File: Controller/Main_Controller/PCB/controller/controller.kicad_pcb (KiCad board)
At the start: 2 copper layers, 99.1 x 99.1 mm, 64 parts, among them J1 nRF24L01_Conn, Q1 S9013, Q2 S9013, Q3 S9013, SW1 SW_SPDT, U1 Joystick, U2 Joystick, U3 ZSR330GTA, U4 LM358DR2G, U5 ZLDO1117G50TA

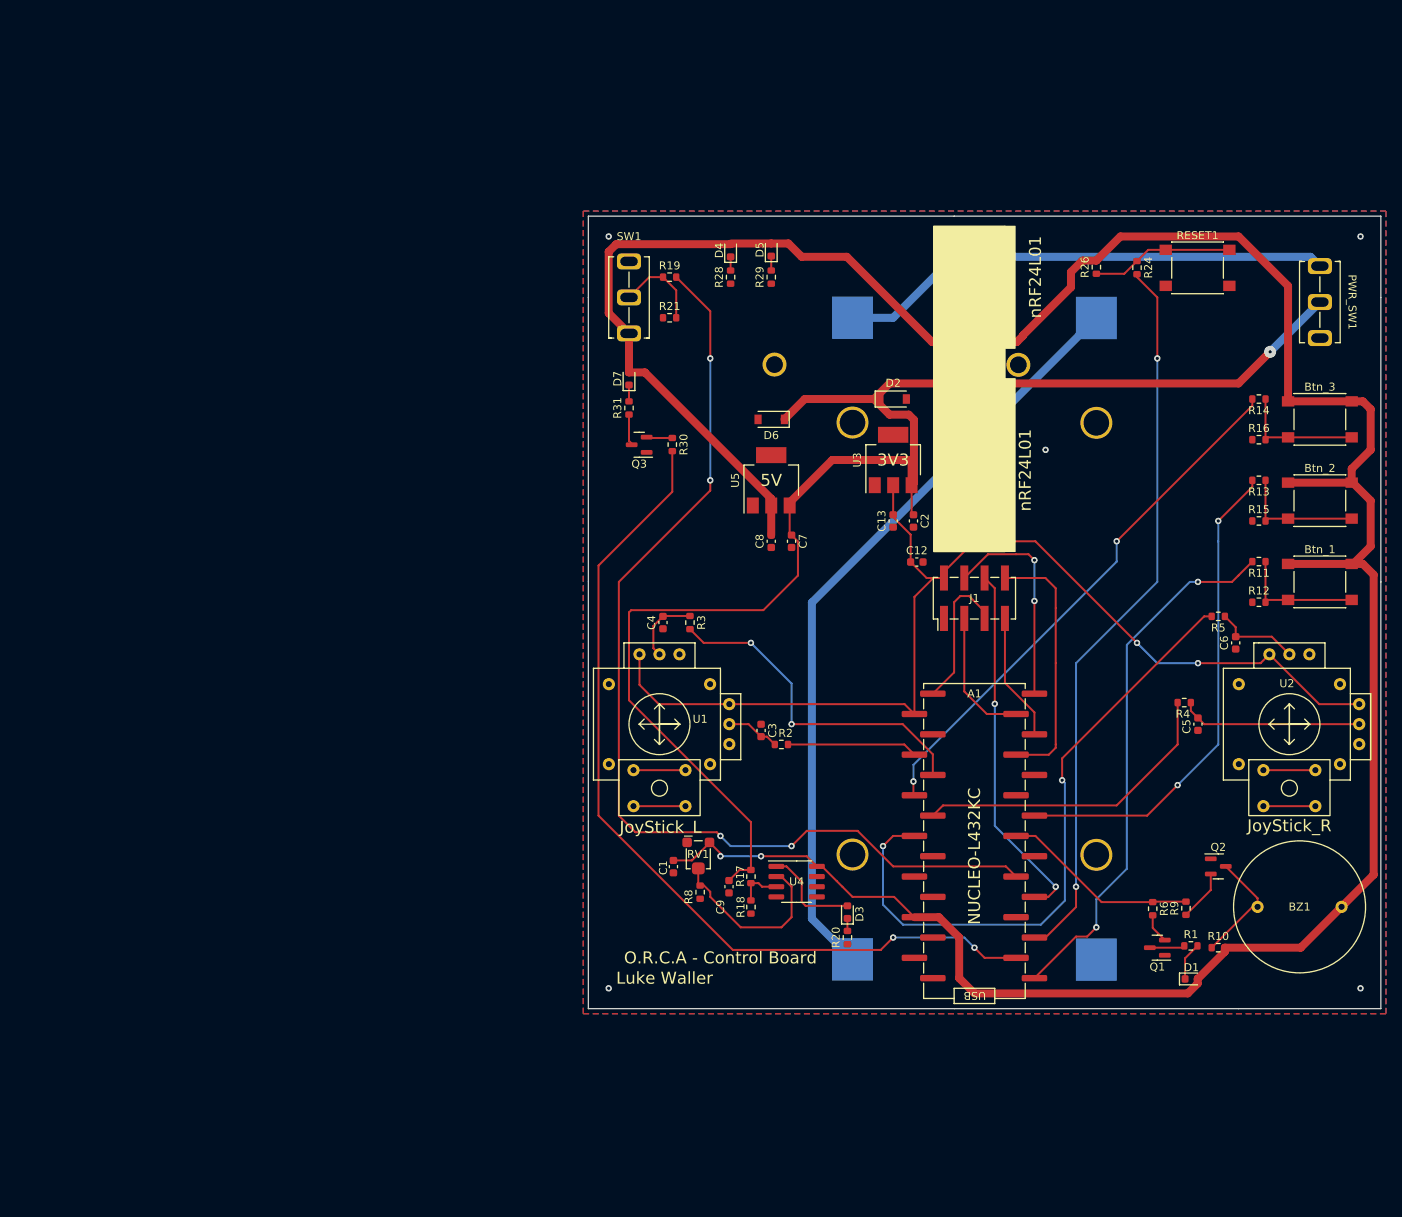
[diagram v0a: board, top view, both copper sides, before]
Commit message: Finished footprints on the schematic.
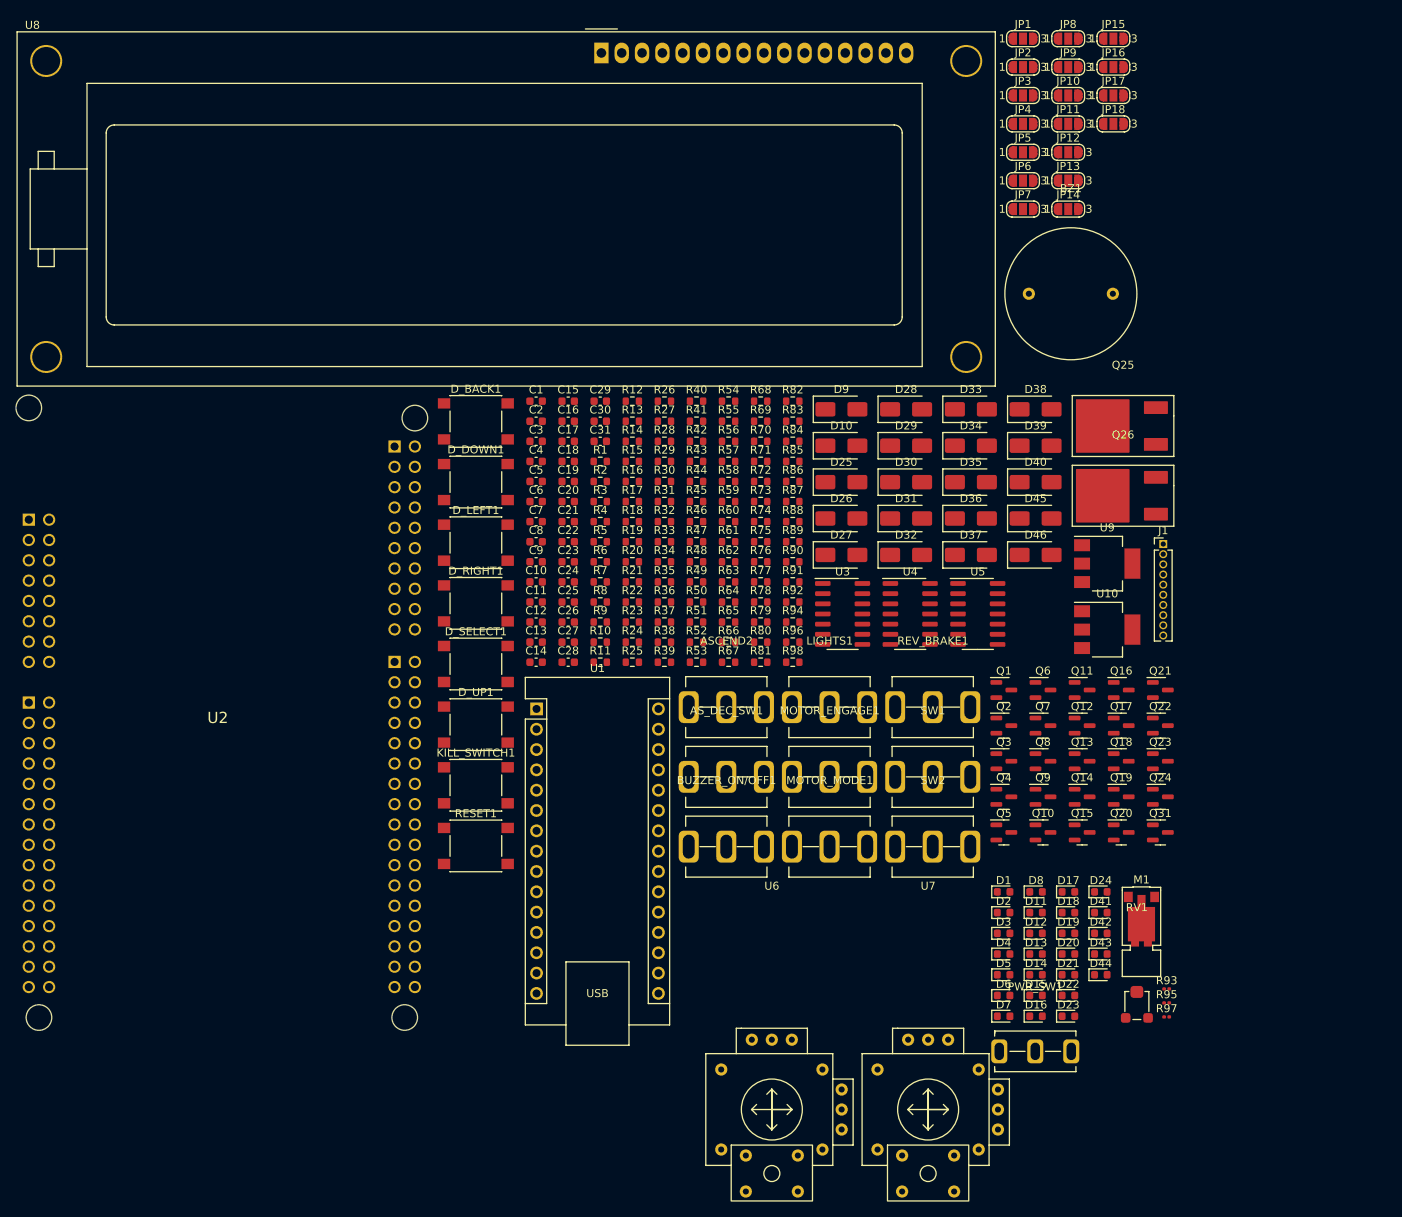
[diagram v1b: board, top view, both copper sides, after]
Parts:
- removed A1: NUCLEO-L432KC, My_library:NUCELO-L432KC_SMD
- removed BT1, BT2: Bat_18650, My_library:18650_Holder(1)
- removed Btn_1, Btn_2, Btn_3: SW_SPST, Button_Switch_SMD:SW_Push_1P1T_NO_6x6mm_H9.5mm
- added ASCEND2: SW_SPDT, My_library:1Ms1T1B1M1QE, F.Cu at (123.9, 112.2)
- added AS_DEC_SW1: SW_SPDT_MSM, My_library:1Ms1T1B1M1QE, F.Cu at (123.9, 120.9)
- added BUZZER_ON/OFF1: SW_SPDT, My_library:1Ms1T1B1M1QE, F.Cu at (123.9, 129.6)
- added C10: 100nF, Capacitor_SMD:C_0603_1608Metric, F.Cu at (100.2, 96.5)
- added C11: 100nF, Capacitor_SMD:C_0603_1608Metric, F.Cu at (100.2, 99.0)
- added C14: 100nF, Capacitor_SMD:C_0603_1608Metric, F.Cu at (100.2, 106.6)
- added C15: 100nF, Capacitor_SMD:C_0603_1608Metric, F.Cu at (104.2, 73.9)
- added C16: 100nF, Capacitor_SMD:C_0603_1608Metric, F.Cu at (104.2, 76.4)
- added C17: 100nF, Capacitor_SMD:C_0603_1608Metric, F.Cu at (104.2, 78.9)
- added C18: 100nF, Capacitor_SMD:C_0603_1608Metric, F.Cu at (104.2, 81.5)
- added C19: 100nF, Capacitor_SMD:C_0603_1608Metric, F.Cu at (104.2, 84.0)
- added C20: 100nF, Capacitor_SMD:C_0603_1608Metric, F.Cu at (104.2, 86.5)
- added C21: 100nF, Capacitor_SMD:C_0603_1608Metric, F.Cu at (104.2, 89.0)
- added C22: 100nF, Capacitor_SMD:C_0603_1608Metric, F.Cu at (104.2, 91.5)
- added C23: 100nF, Capacitor_SMD:C_0603_1608Metric, F.Cu at (104.2, 94.0)
- added C24: 100nF, Capacitor_SMD:C_0603_1608Metric, F.Cu at (104.2, 96.5)
- added C25: 100nF, Capacitor_SMD:C_0603_1608Metric, F.Cu at (104.2, 99.0)
- added C26: 100nF, Capacitor_SMD:C_0603_1608Metric, F.Cu at (104.2, 101.5)
- added C27: 100nF, Capacitor_SMD:C_0603_1608Metric, F.Cu at (104.2, 104.0)
- added C28: 100nF, Capacitor_SMD:C_0603_1608Metric, F.Cu at (104.2, 106.6)
- added C29: 100nF, Capacitor_SMD:C_0603_1608Metric, F.Cu at (108.2, 73.9)
- added C30: 100nF, Capacitor_SMD:C_0603_1608Metric, F.Cu at (108.2, 76.4)
- added C31: 100nF, Capacitor_SMD:C_0603_1608Metric, F.Cu at (108.2, 78.9)
- added D10: D, Diode_SMD:D_SMA, F.Cu at (138.3, 79.5)
- added D11: BLUE, LED_SMD:LED_0603_1608Metric, F.Cu at (162.6, 137.9)
- added D12: WHITE, LED_SMD:LED_0603_1608Metric, F.Cu at (162.6, 140.4)
- added D13: WHITE, LED_SMD:LED_0603_1608Metric, F.Cu at (162.6, 143.0)
- added D14: RED, LED_SMD:LED_0603_1608Metric, F.Cu at (162.6, 145.6)
- added D15: RED, LED_SMD:LED_0603_1608Metric, F.Cu at (162.6, 148.2)
- added D16: RED, LED_SMD:LED_0603_1608Metric, F.Cu at (162.6, 150.8)
- added D17: RED, LED_SMD:LED_0603_1608Metric, F.Cu at (166.7, 135.3)
- added D18: GREEN, LED_SMD:LED_0603_1608Metric, F.Cu at (166.7, 137.9)
- added D19: RED, LED_SMD:LED_0603_1608Metric, F.Cu at (166.7, 140.4)
- added D20: RED, LED_SMD:LED_0603_1608Metric, F.Cu at (166.7, 143.0)
- added D21: BLUE, LED_SMD:LED_0603_1608Metric, F.Cu at (166.7, 145.6)
- added D22: RED, LED_SMD:LED_0603_1608Metric, F.Cu at (166.7, 148.2)
- added D23: RED, LED_SMD:LED_0603_1608Metric, F.Cu at (166.7, 150.8)
- added D24: RED, LED_SMD:LED_0603_1608Metric, F.Cu at (170.7, 135.3)
- added D25: D, Diode_SMD:D_SMA, F.Cu at (138.3, 84.0)
- added D26: D, Diode_SMD:D_SMA, F.Cu at (138.3, 88.6)
- added D27: D, Diode_SMD:D_SMA, F.Cu at (138.3, 93.1)
- added D28: D, Diode_SMD:D_SMA, F.Cu at (146.4, 74.9)
- added D29: D, Diode_SMD:D_SMA, F.Cu at (146.4, 79.5)
- added D30: D, Diode_SMD:D_SMA, F.Cu at (146.4, 84.0)
- added D31: D, Diode_SMD:D_SMA, F.Cu at (146.4, 88.6)
- added D32: D, Diode_SMD:D_SMA, F.Cu at (146.4, 93.1)
- added D33: D, Diode_SMD:D_SMA, F.Cu at (154.5, 74.9)
- added D34: D, Diode_SMD:D_SMA, F.Cu at (154.5, 79.5)
- added D35: D, Diode_SMD:D_SMA, F.Cu at (154.5, 84.0)
- added D36: D, Diode_SMD:D_SMA, F.Cu at (154.5, 88.6)
- added D37: D, Diode_SMD:D_SMA, F.Cu at (154.5, 93.1)
- added D38: D, Diode_SMD:D_SMA, F.Cu at (162.6, 74.9)
- added D39: D, Diode_SMD:D_SMA, F.Cu at (162.6, 79.5)
- added D40: D, Diode_SMD:D_SMA, F.Cu at (162.6, 84.0)
- added D41: YELLOW, LED_SMD:LED_0603_1608Metric, F.Cu at (170.7, 137.9)
- added D42: BLUE, LED_SMD:LED_0603_1608Metric, F.Cu at (170.7, 140.4)
- added D43: GREEN, LED_SMD:LED_0603_1608Metric, F.Cu at (170.7, 143.0)
- added D44: BLUE, LED_SMD:LED_0603_1608Metric, F.Cu at (170.7, 145.6)
- added D45: D, Diode_SMD:D_SMA, F.Cu at (162.6, 88.6)
- added D46: D, Diode_SMD:D_SMA, F.Cu at (162.6, 93.1)
- added D8: RED, LED_SMD:LED_0603_1608Metric, F.Cu at (162.6, 135.3)
- added D9: D, Diode_SMD:D_SMA, F.Cu at (138.3, 74.9)
- added D_BACK1: SW_SPST, Button_Switch_SMD:SW_Push_1P1T_NO_6x6mm_H9.5mm, F.Cu at (92.6, 76.5)
- added D_DOWN1: SW_SPST, Button_Switch_SMD:SW_Push_1P1T_NO_6x6mm_H9.5mm, F.Cu at (92.6, 84.0)
- added D_LEFT1: SW_SPST, Button_Switch_SMD:SW_Push_1P1T_NO_6x6mm_H9.5mm, F.Cu at (92.6, 91.6)
- added D_RIGHT1: SW_SPST, Button_Switch_SMD:SW_Push_1P1T_NO_6x6mm_H9.5mm, F.Cu at (92.6, 99.2)
- added D_SELECT1: SW_SPST, Button_Switch_SMD:SW_Push_1P1T_NO_6x6mm_H9.5mm, F.Cu at (92.6, 106.8)
- added D_UP1: SW_SPST, Button_Switch_SMD:SW_Push_1P1T_NO_6x6mm_H9.5mm, F.Cu at (92.6, 114.4)
- added JP1: SolderJumper_3_Open, Jumper:SolderJumper-3_P1.3mm_Open_RoundedPad1.0x1.5mm_NumberLabels, F.Cu at (161.0, 28.6)
- added JP10: SolderJumper_3_Open, Jumper:SolderJumper-3_P1.3mm_Open_RoundedPad1.0x1.5mm_NumberLabels, F.Cu at (166.7, 35.7)
- added JP11: SolderJumper_3_Open, Jumper:SolderJumper-3_P1.3mm_Open_RoundedPad1.0x1.5mm_NumberLabels, F.Cu at (166.7, 39.3)
- added JP12: SolderJumper_3_Open, Jumper:SolderJumper-3_P1.3mm_Open_RoundedPad1.0x1.5mm_NumberLabels, F.Cu at (166.7, 42.8)
- added JP13: SolderJumper_3_Open, Jumper:SolderJumper-3_P1.3mm_Open_RoundedPad1.0x1.5mm_NumberLabels, F.Cu at (166.7, 46.4)
- added JP14: SolderJumper_3_Open, Jumper:SolderJumper-3_P1.3mm_Open_RoundedPad1.0x1.5mm_NumberLabels, F.Cu at (166.7, 49.9)
- added JP15: SolderJumper_3_Open, Jumper:SolderJumper-3_P1.3mm_Open_RoundedPad1.0x1.5mm_NumberLabels, F.Cu at (172.3, 28.6)
- added JP16: SolderJumper_3_Open, Jumper:SolderJumper-3_P1.3mm_Open_RoundedPad1.0x1.5mm_NumberLabels, F.Cu at (172.3, 32.2)
- added JP17: SolderJumper_3_Open, Jumper:SolderJumper-3_P1.3mm_Open_RoundedPad1.0x1.5mm_NumberLabels, F.Cu at (172.3, 35.7)
- added JP18: SolderJumper_3_Open, Jumper:SolderJumper-3_P1.3mm_Open_RoundedPad1.0x1.5mm_NumberLabels, F.Cu at (172.3, 39.3)
- added JP2: SolderJumper_3_Open, Jumper:SolderJumper-3_P1.3mm_Open_RoundedPad1.0x1.5mm_NumberLabels, F.Cu at (161.0, 32.2)
- added JP3: SolderJumper_3_Open, Jumper:SolderJumper-3_P1.3mm_Open_RoundedPad1.0x1.5mm_NumberLabels, F.Cu at (161.0, 35.7)
- added JP4: SolderJumper_3_Open, Jumper:SolderJumper-3_P1.3mm_Open_RoundedPad1.0x1.5mm_NumberLabels, F.Cu at (161.0, 39.3)
- added JP5: SolderJumper_3_Open, Jumper:SolderJumper-3_P1.3mm_Open_RoundedPad1.0x1.5mm_NumberLabels, F.Cu at (161.0, 42.8)
- added JP6: SolderJumper_3_Open, Jumper:SolderJumper-3_P1.3mm_Open_RoundedPad1.0x1.5mm_NumberLabels, F.Cu at (161.0, 46.4)
- added JP7: SolderJumper_3_Open, Jumper:SolderJumper-3_P1.3mm_Open_RoundedPad1.0x1.5mm_NumberLabels, F.Cu at (161.0, 49.9)
- added JP8: SolderJumper_3_Open, Jumper:SolderJumper-3_P1.3mm_Open_RoundedPad1.0x1.5mm_NumberLabels, F.Cu at (166.7, 28.6)
- added JP9: SolderJumper_3_Open, Jumper:SolderJumper-3_P1.3mm_Open_RoundedPad1.0x1.5mm_NumberLabels, F.Cu at (166.7, 32.2)
- added KILL_SWITCH1: SW_SPST, Button_Switch_SMD:SW_Push_1P1T_NO_6x6mm_H9.5mm, F.Cu at (92.6, 121.9)
- added LIGHTS1: SW_SPDT, My_library:1Ms1T1B1M1QE, F.Cu at (136.8, 112.2)
- added M1: Motor_DC, Motors:Vybronics_VZ30C1T8219732L, F.Cu at (175.8, 140.2)
- added MOTOR_ENGAGE1: SW_SPDT, My_library:1Ms1T1B1M1QE, F.Cu at (136.8, 120.9)
- added MOTOR_MODE1: SW_SPDT, My_library:1Ms1T1B1M1QE, F.Cu at (136.8, 129.6)
- added Q10: BC817, Package_TO_SOT_SMD:SOT-23, F.Cu at (163.5, 127.8)
- added Q11: BC817, Package_TO_SOT_SMD:SOT-23, F.Cu at (168.4, 110.0)
- added Q12: BC817, Package_TO_SOT_SMD:SOT-23, F.Cu at (168.4, 114.5)
- added Q13: BC817, Package_TO_SOT_SMD:SOT-23, F.Cu at (168.4, 118.9)
- added Q14: BC817, Package_TO_SOT_SMD:SOT-23, F.Cu at (168.4, 123.4)
- added Q15: BC817, Package_TO_SOT_SMD:SOT-23, F.Cu at (168.4, 127.8)
- added Q16: BC817, Package_TO_SOT_SMD:SOT-23, F.Cu at (173.3, 110.0)
- added Q17: BC817, Package_TO_SOT_SMD:SOT-23, F.Cu at (173.3, 114.5)
- added Q18: BC817, Package_TO_SOT_SMD:SOT-23, F.Cu at (173.3, 118.9)
- added Q19: BC817, Package_TO_SOT_SMD:SOT-23, F.Cu at (173.3, 123.4)
- added Q20: BC817, Package_TO_SOT_SMD:SOT-23, F.Cu at (173.3, 127.8)
- added Q21: BC817, Package_TO_SOT_SMD:SOT-23, F.Cu at (178.2, 110.0)
- added Q22: BC817, Package_TO_SOT_SMD:SOT-23, F.Cu at (178.2, 114.5)
- added Q23: BC817, Package_TO_SOT_SMD:SOT-23, F.Cu at (178.2, 118.9)
- added Q24: BC817, Package_TO_SOT_SMD:SOT-23, F.Cu at (178.2, 123.4)
- added Q25: IRFR9014PBF, My_library:STD20NF06L, F.Cu at (171.0, 77.0)
- added Q26: STD20NF06L, My_library:STD20NF06L, F.Cu at (171.0, 85.8)
- added Q31: BC817, Package_TO_SOT_SMD:SOT-23, F.Cu at (178.2, 127.8)
- added Q4: BC817, Package_TO_SOT_SMD:SOT-23, F.Cu at (158.6, 123.4)
- added Q5: BC817, Package_TO_SOT_SMD:SOT-23, F.Cu at (158.6, 127.8)
- added Q6: BC817, Package_TO_SOT_SMD:SOT-23, F.Cu at (163.5, 110.0)
- added Q7: BC817, Package_TO_SOT_SMD:SOT-23, F.Cu at (163.5, 114.5)
- added Q8: BC817, Package_TO_SOT_SMD:SOT-23, F.Cu at (163.5, 118.9)
- added Q9: BC817, Package_TO_SOT_SMD:SOT-23, F.Cu at (163.5, 123.4)
- added R22: 4K7, Resistor_SMD:R_0603_1608Metric, F.Cu at (112.2, 99.0)
- added R23: 4K7, Resistor_SMD:R_0603_1608Metric, F.Cu at (112.2, 101.5)
- added R25: 4K7, Resistor_SMD:R_0603_1608Metric, F.Cu at (112.2, 106.6)
- added R27: 1K, Resistor_SMD:R_0603_1608Metric, F.Cu at (116.2, 76.4)
- added R32: 150, Resistor_SMD:R_0603_1608Metric, F.Cu at (116.2, 89.0)
- added R33: 4K7, Resistor_SMD:R_0603_1608Metric, F.Cu at (116.2, 91.5)
- added R34: 4K7, Resistor_SMD:R_0603_1608Metric, F.Cu at (116.2, 94.0)
- added R35: 4K7, Resistor_SMD:R_0603_1608Metric, F.Cu at (116.2, 96.5)
- added R36: 4K7, Resistor_SMD:R_0603_1608Metric, F.Cu at (116.2, 99.0)
- added R37: 150, Resistor_SMD:R_0603_1608Metric, F.Cu at (116.2, 101.5)
- added R38: 2K2, Resistor_SMD:R_0603_1608Metric, F.Cu at (116.2, 104.0)
- added R39: 150, Resistor_SMD:R_0603_1608Metric, F.Cu at (116.2, 106.6)
- added R40: 150, Resistor_SMD:R_0603_1608Metric, F.Cu at (120.2, 73.9)
- added R41: 4K7, Resistor_SMD:R_0603_1608Metric, F.Cu at (120.2, 76.4)
- added R42: 4K7, Resistor_SMD:R_0603_1608Metric, F.Cu at (120.2, 78.9)
- added R43: 4K7, Resistor_SMD:R_0603_1608Metric, F.Cu at (120.2, 81.5)
- added R44: 4K7, Resistor_SMD:R_0603_1608Metric, F.Cu at (120.2, 84.0)
- added R45: 1K, Resistor_SMD:R_0603_1608Metric, F.Cu at (120.2, 86.5)
- added R46: 150, Resistor_SMD:R_0603_1608Metric, F.Cu at (120.2, 89.0)
- added R47: 150, Resistor_SMD:R_0603_1608Metric, F.Cu at (120.2, 91.5)
- added R48: 150, Resistor_SMD:R_0603_1608Metric, F.Cu at (120.2, 94.0)
- added R49: 47K, Resistor_SMD:R_0603_1608Metric, F.Cu at (120.2, 96.5)
- added R50: 47K, Resistor_SMD:R_0603_1608Metric, F.Cu at (120.2, 99.0)
- added R51: 47K, Resistor_SMD:R_0603_1608Metric, F.Cu at (120.2, 101.5)
- added R52: 47K, Resistor_SMD:R_0603_1608Metric, F.Cu at (120.2, 104.0)
- added R53: 47K, Resistor_SMD:R_0603_1608Metric, F.Cu at (120.2, 106.6)
- added R54: 47K, Resistor_SMD:R_0603_1608Metric, F.Cu at (124.2, 73.9)
- added R55: 47K, Resistor_SMD:R_0603_1608Metric, F.Cu at (124.2, 76.4)
- added R56: 47K, Resistor_SMD:R_0603_1608Metric, F.Cu at (124.2, 78.9)
- added R57: 47K, Resistor_SMD:R_0603_1608Metric, F.Cu at (124.2, 81.5)
- added R58: 47K, Resistor_SMD:R_0603_1608Metric, F.Cu at (124.2, 84.0)
- added R59: 47K, Resistor_SMD:R_0603_1608Metric, F.Cu at (124.2, 86.5)
- added R60: 47K, Resistor_SMD:R_0603_1608Metric, F.Cu at (124.2, 89.0)
- added R61: 47K, Resistor_SMD:R_0603_1608Metric, F.Cu at (124.2, 91.5)
- added R62: 47K, Resistor_SMD:R_0603_1608Metric, F.Cu at (124.2, 94.0)
- added R63: 47K, Resistor_SMD:R_0603_1608Metric, F.Cu at (124.2, 96.5)
- added R64: 47K, Resistor_SMD:R_0603_1608Metric, F.Cu at (124.2, 99.0)
- added R65: 47K, Resistor_SMD:R_0603_1608Metric, F.Cu at (124.2, 101.5)
- added R66: 47K, Resistor_SMD:R_0603_1608Metric, F.Cu at (124.2, 104.0)
- added R67: 47K, Resistor_SMD:R_0603_1608Metric, F.Cu at (124.2, 106.6)
- added R68: 47K, Resistor_SMD:R_0603_1608Metric, F.Cu at (128.2, 73.9)
- added R69: 47K, Resistor_SMD:R_0603_1608Metric, F.Cu at (128.2, 76.4)
- added R7: 4K7, Resistor_SMD:R_0603_1608Metric, F.Cu at (108.2, 96.5)
- added R70: 47K, Resistor_SMD:R_0603_1608Metric, F.Cu at (128.2, 78.9)
- added R71: 47K, Resistor_SMD:R_0603_1608Metric, F.Cu at (128.2, 81.5)
- added R72: 47K, Resistor_SMD:R_0603_1608Metric, F.Cu at (128.2, 84.0)
- added R73: 47K, Resistor_SMD:R_0603_1608Metric, F.Cu at (128.2, 86.5)
- added R74: 47K, Resistor_SMD:R_0603_1608Metric, F.Cu at (128.2, 89.0)
- added R75: 620, Resistor_SMD:R_0603_1608Metric, F.Cu at (128.2, 91.5)
- added R76: 620, Resistor_SMD:R_0603_1608Metric, F.Cu at (128.2, 94.0)
- added R77: 620, Resistor_SMD:R_0603_1608Metric, F.Cu at (128.2, 96.5)
- added R78: 620, Resistor_SMD:R_0603_1608Metric, F.Cu at (128.2, 99.0)
- added R79: 47K, Resistor_SMD:R_0603_1608Metric, F.Cu at (128.2, 101.5)
- added R80: 47K, Resistor_SMD:R_0603_1608Metric, F.Cu at (128.2, 104.0)
- added R81: 47K, Resistor_SMD:R_0603_1608Metric, F.Cu at (128.2, 106.6)
- added R82: 47K, Resistor_SMD:R_0603_1608Metric, F.Cu at (132.2, 73.9)
- added R83: 47K, Resistor_SMD:R_0603_1608Metric, F.Cu at (132.2, 76.4)
- added R84: 47K, Resistor_SMD:R_0603_1608Metric, F.Cu at (132.2, 78.9)
- added R85: 2K2, Resistor_SMD:R_0603_1608Metric, F.Cu at (132.2, 81.5)
- added R86: 1K, Resistor_SMD:R_0603_1608Metric, F.Cu at (132.2, 84.0)
- added R87: 4K7, Resistor_SMD:R_0603_1608Metric, F.Cu at (132.2, 86.5)
- added R88: 2K2, Resistor_SMD:R_0603_1608Metric, F.Cu at (132.2, 89.0)
- added R89: 2K2, Resistor_SMD:R_0603_1608Metric, F.Cu at (132.2, 91.5)
- added R90: 1K, Resistor_SMD:R_0603_1608Metric, F.Cu at (132.2, 94.0)
- added R91: 10K, Resistor_SMD:R_0603_1608Metric, F.Cu at (132.2, 96.5)
- added R92: 4K7, Resistor_SMD:R_0603_1608Metric, F.Cu at (132.2, 99.0)
- added R93: 1K, Resistor_SMD:R_0201_0603Metric, F.Cu at (179.0, 147.4)
- added R94: 4K7, Resistor_SMD:R_0603_1608Metric, F.Cu at (132.2, 101.5)
- added R95: 100K, Resistor_SMD:R_0201_0603Metric, F.Cu at (179.0, 149.1)
- added R96: 220R, Resistor_SMD:R_0603_1608Metric, F.Cu at (132.2, 104.0)
- added R97: 100R, Resistor_SMD:R_0201_0603Metric, F.Cu at (179.0, 150.9)
- added R98: 10K, Resistor_SMD:R_0603_1608Metric, F.Cu at (132.2, 106.6)
- added REV_BRAKE1: SW_SPDT, My_library:1Ms1T1B1M1QE, F.Cu at (149.7, 112.2)
- added SW2: SW_SPDT, My_library:1Ms1T1B1M1QE, F.Cu at (149.7, 129.6)
- added U10: ZLDO1117G50TA, Package_TO_SOT_SMD:SOT-223, F.Cu at (171.5, 102.5)
- added U6: Joystick, My_library:Joystick, F.Cu at (129.6, 162.5)
- added U7: Joystick, My_library:Joystick, F.Cu at (149.2, 162.5)
- added U8: HY1602E, Display:HY1602E, F.Cu at (108.3, 30.4)
- added U9: ZSR330GTA, Package_TO_SOT_SMD:SOT-223, F.Cu at (171.5, 94.2)
- D1: value GREEN -> BLUE
- D2, D6: value B5817W-5819W -> GREEN; footprint Diode_SMD:D_SOD-123 -> LED_SMD:LED_0603_1608Metric
- D3, D4: value YELLOW -> RED
- D5: value BLUE -> WHITE
- D7: value BLUE -> RED
- J1: value nRF24L01_Conn -> Conn_01x10; footprint Connector_PinHeader_2.54mm:PinHeader_2x04_P2.54mm_Vertical_SMD -> Connector_PinHeader_1.27mm:PinHeader_1x10_P1.27mm_Vertical
- Q1, Q2, Q3: value S9013 -> BC817
- R1, R24: value 2K2 -> 4K7
- R10, R21, R26: value 10K -> 4K7
- R11: value 2K2 -> 150
- R12, R15, R16: value 10K -> 150
- R13, R28: value 2K2 -> 390
- R17, R18: value 100K -> 47K
- R19, R20: value 2K2 -> 47K
- R2: value 620 -> 1K
- R29: value 1K -> 390
- R3, R5: value 620 -> 4K7
- R30: value 4K7 -> 150
- R31: value 1K -> 150
- R4: value 620 -> 2K2
- R8: value 40K -> 4K7
- SW1: footprint My_library:KNX-1-D1 -> My_library:1Ms1T1B1M1QE
- U1: value Joystick -> NUCLEO-L432KC; footprint My_library:Joystick -> Module:Arduino_Nano
- U2: value Joystick -> NUCLEO144-F429ZI; footprint My_library:Joystick -> My_library:MODULE_NUCLEO-F429ZI_JUST_PINS
- U3: value ZSR330GTA -> 74HC14; footprint Package_TO_SOT_SMD:SOT-223 -> Package_SO:SO-14_3.9x8.65mm_P1.27mm
- U4: value LM358DR2G -> 74HC14; footprint Package_SO:SOP-8_3.76x4.96mm_P1.27mm -> Package_SO:SO-14_3.9x8.65mm_P1.27mm
- U5: value ZLDO1117G50TA -> 74HC14; footprint Package_TO_SOT_SMD:SOT-223 -> Package_SO:SO-14_3.9x8.65mm_P1.27mm
- moved U2 133.4 mm to (60.9, 113.5)
- moved RESET1 115.6 mm to (92.6, 129.5)
- moved PWR_SW1 100.2 mm to (162.5, 155.2), turned to 0 degrees
- moved R1 95.5 mm to (108.2, 81.5)
- moved D5 95.2 mm to (158.6, 145.6), turned to 0 degrees
- moved D4 94.3 mm to (158.6, 143.0), turned to 0 degrees
- moved D7 92.4 mm to (158.6, 150.8), turned to 0 degrees
- moved C6 89.2 mm to (100.2, 86.5), turned to 0 degrees
- moved C5 88.1 mm to (100.2, 84.0), turned to 0 degrees
- moved R10 86.2 mm to (108.2, 104.0)
- moved R11 83.3 mm to (108.2, 106.6), turned to 0 degrees
- moved R12 82.3 mm to (112.2, 73.9)
- moved BZ1 81.8 mm to (167.0, 60.5), turned to 0 degrees
- moved R6 81.5 mm to (108.2, 94.0), turned to 0 degrees
- moved R9 81.5 mm to (108.2, 101.5), turned to 0 degrees
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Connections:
- BZ1 pad 1: +5V -> Net-(BUZZER_ON/OFF1-A)
- BZ1 pad 2: Net-(BZ1-Pad2) -> Net-(BZ1-+)
- C1 pad 1: +5V -> Earth
- C1 pad 2: Earth -> SWITCH_1_SB
- C12 pad 1: +3V3 -> Earth
- C12 pad 2: Earth -> MOTOR_DENGAGE_SB
- C13 pad 1: Earth -> +3V3
- C13 pad 2: +3V3 -> Earth
- C2 pad 1: BAT_PWR -> Earth
- C2 pad 2: Earth -> SWITCH_2_SB
- C3 pad 2: Net-(C3-Pad2) -> MOTOR_MODE_1_SB
- C4 pad 2: Net-(C4-Pad2) -> MOTOR_MODE_2_SB
- C5 pad 2: Net-(C5-Pad2) -> KILL_SWITCH_SB
- C6 pad 2: Net-(C6-Pad2) -> ASCEND_SB
- C7 pad 1: BAT_PWR -> Earth
- C7 pad 2: Earth -> DESCEND_SB
- C8 pad 2: +5V -> LIGHTS_SB
- C9 pad 1: BAT_PWR -> Earth
- C9 pad 2: Earth -> BRAKE_MODE_SB
- D1 pad 1: Net-(D1-Pad1) -> Net-(D1-K)
- D2 pad 1: BAT_PWR -> Net-(D2-K)
- D2 pad 2: Earth -> +5V
- D3 pad 1: Net-(D3-Pad1) -> Net-(D3-K)
- D3 pad 2: Net-(D3-Pad2) -> +5V
- D4 pad 1: Net-(D4-Pad1) -> Net-(D4-K)
- D5 pad 1: Net-(D5-Pad1) -> Net-(D5-K)
- D6 pad 1: BAT_PWR -> Net-(D6-K)
- D6 pad 2: Earth -> +5V
- D7 pad 1: Net-(D7-Pad1) -> Net-(D7-K)
- J1 pad 1: Earth -> VIN
- J1 pad 2: +3V3 -> MOSI_1
- J1 pad 3: NRF_CE -> MISO_1
- J1 pad 4: NRF_CSN -> CLK_1
- J1 pad 5: NRF_SCK -> MOSI_2
- J1 pad 6: NRF_MOSI -> MISO_2
- J1 pad 7: NRF_MISO -> CLK_2
- J1 pad 8: NRF_IRQ -> DET_IN
- PWR_SW1 pad 1: +BATT -> +12V
- PWR_SW1 pad 2: BAT_PWR -> Net-(D45-K)
- Q1 pad 1: Earth -> Net-(Q1-B)
- Q1 pad 2: Net-(Q1-Pad2) -> Earth
- Q1 pad 3: Net-(Q1-Pad3) -> Net-(Q1-C)
- Q2 pad 1: Earth -> Net-(Q2-B)
- Q2 pad 2: Net-(Q2-Pad2) -> Earth
- Q2 pad 3: Net-(BZ1-Pad2) -> Net-(Q2-C)
- Q3 pad 1: Earth -> Net-(Q3-B)
- Q3 pad 2: Net-(Q3-Pad2) -> Earth
- Q3 pad 3: Net-(Q3-Pad3) -> Net-(Q3-C)
- R1 pad 1: Net-(Q1-Pad3) -> Net-(Q1-B)
- R1 pad 2: Net-(D1-Pad1) -> MOTOR_MODE_1_LED
- R10 pad 1: Net-(BZ1-Pad2) -> Net-(Q18-B)
- R10 pad 2: +5V -> COL_SENS_7
- R11 pad 1: Net-(Btn_1-Pad2) -> Net-(Q3-C)
- R11 pad 2: Btn_1 -> Net-(D3-K)
- R12 pad 1: Earth -> Net-(Q4-C)
- R12 pad 2: Net-(Btn_1-Pad2) -> Net-(D4-K)
- R13 pad 1: Net-(Btn_2-Pad2) -> Net-(Q5-C)
- R13 pad 2: Btn_2 -> Net-(D5-K)
- R14 pad 1: Net-(Btn_3-Pad2) -> Net-(Q6-C)
- R14 pad 2: Btn_3 -> Net-(D6-K)
- R15 pad 1: Earth -> Net-(Q7-C)
- R15 pad 2: Net-(Btn_2-Pad2) -> Net-(D7-K)
- R16 pad 1: Earth -> Net-(Q18-C)
- R16 pad 2: Net-(Btn_3-Pad2) -> Net-(D8-K)
- R17 pad 1: Net-(R17-Pad1) -> Net-(D9-A)
- R17 pad 2: BAT_PWR -> +5V
- R18 pad 1: Earth -> Net-(D10-A)
- R18 pad 2: Net-(R17-Pad1) -> +5V
- R19 pad 1: Net-(R19-Pad1) -> SWITCH_1_SB
- R19 pad 2: SW_1 -> Net-(D9-A)
- R2 pad 1: Net-(C3-Pad2) -> Net-(Q1-C)
- R2 pad 2: L_PITCH -> Net-(D1-K)
- R20 pad 1: Earth -> SWITCH_2_SB
- R20 pad 2: Net-(D3-Pad1) -> Net-(D10-A)
- R21 pad 1: Earth -> Net-(Q9-B)
- R21 pad 2: Net-(R19-Pad1) -> ASCEND_LED
- R24 pad 1: Net-(R24-Pad1) -> Net-(Q12-B)
- R24 pad 2: RESET -> LED_2
- R26 pad 1: Net-(R24-Pad1) -> Net-(Q22-B)
- R26 pad 2: +5V -> COL_SENS_8
- R28 pad 1: Earth -> Net-(Q10-C)
- R28 pad 2: Net-(D4-Pad1) -> Net-(D12-K)
- R29 pad 1: Earth -> Net-(Q11-C)
- R29 pad 2: Net-(D5-Pad1) -> Net-(D13-K)
- R3 pad 1: Net-(C4-Pad2) -> Net-(Q2-B)
- R3 pad 2: L_ROLL -> MOTOR_MODE_2_LED
- R30 pad 1: Net-(Q3-Pad2) -> Net-(Q12-C)
- R30 pad 2: LED_1 -> Net-(D14-K)
- R31 pad 1: Net-(Q3-Pad3) -> Net-(Q8-C)
- R31 pad 2: Net-(D7-Pad1) -> Net-(D15-K)
- R4 pad 1: Net-(C5-Pad2) -> Net-(Q2-C)
- R4 pad 2: R_PITCH -> Net-(D2-K)
- R5 pad 1: Net-(C6-Pad2) -> Net-(Q3-B)
- R5 pad 2: R_ROLL -> KILL_SWTICH_LED
- R6 pad 1: BUZZER -> Net-(Q4-B)
- R6 pad 2: Net-(Q1-Pad2) -> BRAKE_LED
- R8 pad 1: Earth -> Net-(Q6-B)
- R8 pad 2: Net-(R8-Pad2) -> LED_1
- R9 pad 1: Net-(Q2-Pad2) -> Net-(Q7-B)
- R9 pad 2: BUZZER -> COL_SENS_3
- RESET1 pad 1: Net-(R24-Pad1) -> Net-(RESET1-A)
- RV1 pad 1: +5V -> Earth
- RV1 pad 2: Net-(R8-Pad2) -> Net-(U8-Vo)
- RV1 pad 3: Earth -> +5V
- SW1 pad 1: +5V -> Net-(D9-A)
- SW1 pad 2: Net-(R19-Pad1) -> Earth
- U3 pad 1: Earth -> MOTOR_MODE_1_SB
- U3 pad 2: +3V3 -> MOTOR_MODE_1
- U3 pad 3: BAT_PWR -> MOTOR_MODE_2_SB
- U3 pad 4: (no net) -> MOTOR_MODE_2
- U4 pad 1: Net-(D3-Pad2) -> BRAKE_MODE_SB
- U4 pad 2: Net-(R8-Pad2) -> BRAKE_MODE
- U4 pad 3: Net-(R17-Pad1) -> REV_MODE_SB
- U4 pad 4: Earth -> REV_MODE
- U4 pad 5: unconnected-(U4-Pad5) -> MOTOR_ENGAGE_SB
- U4 pad 6: unconnected-(U4-Pad6) -> MOTOR_EN
- U4 pad 7: unconnected-(U4-Pad7) -> Earth
- U4 pad 8: +5V -> MOTOR_DE
- U5 pad 1: Earth -> D_UP_SB
- U5 pad 2: +5V -> D_UP
- U5 pad 3: BAT_PWR -> D_DOWN_SB
- U5 pad 4: (no net) -> D_DOWN
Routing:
- net +5V: track 355.1 -> 0.00 mm, vias 2 -> 0
- net BAT_PWR: track 186.1 -> 0.00 mm, vias 1 -> 0
- net +3V3: track 138.1 -> 0.00 mm, vias 2 -> 0
- net SW_1: track 128.2 -> 0.00 mm, vias 4 -> 0
- net LED_1: track 110.2 -> 0.00 mm, vias 2 -> 0
- net Net-(BT1-Pad2): track 97.0 -> 0.00 mm
- net RESET: track 91.1 -> 0.00 mm, vias 2 -> 0
- net R_ROLL: track 80.8 -> 0.00 mm, vias 2 -> 0
- net Btn_1: track 67.3 -> 0.00 mm, vias 2 -> 0
- net Btn_3: track 67.1 -> 0.00 mm, vias 2 -> 0
- net +BATT: track 62.1 -> 0.00 mm
- net Btn_2: track 61.4 -> 0.00 mm, vias 2 -> 0
- net NRF_MOSI: track 45.7 -> 0.00 mm, vias 2 -> 0
- net L_ROLL: track 42.4 -> 0.00 mm, vias 2 -> 0
- net R_PITCH: track 39.5 -> 0.00 mm
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- removed copper zone on B.Cu, net Earth
- removed copper zone on F.Cu, net Earth
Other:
- board outline removed
- board text removed: "3V3"
- board text removed: "5V"
- board text removed: "JoyStick_L"
- board text removed: "JoyStick_R"
- board text removed: "Luke Waller"
- board text removed: "NUCLEO-L432KC"
- board text removed: "O.R.C.A - Control Board"
- board text removed: "nRF24L01"

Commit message: PCB design
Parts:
- KILL_SWITCH1: footprint Button_Switch_SMD:SW_Push_1P1T_NO_6x6mm_H9.5mm -> My_library:Toggle_Switch_10TC605
- Q13, Q14, Q17, Q18, Q21, Q22, Q7, Q8, R10, R25, R26, R35, R36, R43, R44, R9, U1, U2, U5: moved to B.Cu
- R11, R12, R30, R37, R46: value 150 -> 150R
- R13, R28, R29: value 390 -> 390R
- R15, R16, R31, R32, R39, R40, R47, R48: value 150 -> 150R; moved to B.Cu
- R75, R76, R77, R78: value 620 -> 620R
- U8: footprint Display:HY1602E -> My_library:LCD_Display_WH1602B-NYG-JT
- moved R45 302.3 mm to (393.7, -42.4), turned to 90 degrees
- moved R37 298.7 mm to (398.0, 2.54)
- moved R52 297.8 mm to (394.2, -12.7)
- moved D21 297.2 mm to (393.7, -46.2), turned to 90 degrees
- moved R41 295.8 mm to (389.1, -47.0), turned to 180 degrees
- moved C8 295.5 mm to (363.2, -43.2)
- moved C7 294.9 mm to (376.0, -15.2)
- moved R33 291.9 mm to (394.2, 2.54)
- moved C6 290.7 mm to (374.7, -8.89)
- moved AS_DEC_SW1 289.5 mm to (384.0, -6.35)
- moved LIGHTS1 286.9 mm to (378.8, -41.9)
- moved R62 286.3 mm to (393.8, -2.54)
- moved R53 284.1 mm to (384.1, 1.27)
- moved R63 282.7 mm to (390.0, 0.00)
- moved R64 282.4 mm to (368.2, -43.2)
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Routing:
- net D_BACK_SB: track 0.00 -> 93.3 mm, vias 0 -> 1
- net Net-(D39-A): track 0.00 -> 81.9 mm
- net D_DOWN_SB: track 0.00 -> 78.2 mm, vias 0 -> 1
- net D_LEFT_SB: track 0.00 -> 78.2 mm, vias 0 -> 1
- net D_RIGHT_SB: track 0.00 -> 55.3 mm, vias 0 -> 1
- net Net-(BZ1-+): track 0.00 -> 45.6 mm
- net D_UP_SB: track 0.00 -> 41.8 mm, vias 0 -> 1
- net Net-(Q24-C): track 0.00 -> 28.0 mm
- net LCD_D7: track 0.00 -> 27.1 mm
- net Net-(D36-A): track 0.00 -> 27.1 mm
- net Net-(BUZZER_ON/OFF1-A): track 0.00 -> 25.3 mm
- net LCD_D6: track 0.00 -> 25.0 mm
- net LCD_D4: track 0.00 -> 25.0 mm
- net LCD_D5: track 0.00 -> 25.0 mm
- net LCD_RS: track 0.00 -> 25.0 mm
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
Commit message: Tracings complete for the PCB.
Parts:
- added JP19: Jumper_2_Open, My_library:Jumper, F.Cu at (157.0, 24.3)
- added JP20: SolderJumper_2_Open, Jumper:SolderJumper-2_P1.3mm_Open_RoundedPad1.0x1.5mm, F.Cu at (153.6, 24.3)
- KILL_SWITCH1: value SW_SPST -> SW_SPDT; footprint My_library:Toggle_Switch_10TC605 -> My_library:1Ms1T1B1M1QE
- R93, R95, R97: footprint Resistor_SMD:R_0201_0603Metric -> Resistor_SMD:R_0603_1608Metric
- moved D28 293.3 mm to (103.2, 21.8)
- moved R62 292.3 mm to (103.1, 28.1)
- moved R63 290.7 mm to (103.1, 47.2)
- moved R37 287.3 mm to (114.1, 46.4), turned to 90 degrees
- moved R52 287.0 mm to (109.4, 23.1), turned to 90 degrees
- moved D17 286.9 mm to (109.5, 44.7), turned to 180 degrees
- moved Q15 285.8 mm to (115.3, 50.7), turned to 180 degrees
- moved C7 283.9 mm to (98.1, 42.9), turned to -90 degrees
- moved AS_DEC_SW1 283.4 mm to (103.9, 37.0), turned to -90 degrees
- moved C6 279.9 mm to (97.6, 30.2), turned to 90 degrees
- moved R53 279.1 mm to (109.4, 51.0), turned to -90 degrees
- moved R33 278.4 mm to (119.2, 45.5), turned to 90 degrees
- moved JP11 278.2 mm to (96.3, 49.8), turned to -90 degrees
- moved D29 278.0 mm to (103.2, 53.5)
- moved JP7 273.6 mm to (96.3, 23.1), turned to 90 degrees
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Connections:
- J1 pad 8: DET_IN -> Net-(J1-Pin_8)
- J1 pad 9: DET_OUT -> Net-(J1-Pin_9)
- KILL_SWITCH1 pad 1: Earth -> Net-(D27-A)
- KILL_SWITCH1 pad 2: Net-(D27-A) -> Earth
- KILL_SWITCH1 pad 3: (no net) -> unconnected-(KILL_SWITCH1-C-Pad3)
- R5 pad 2: KILL_SWTICH_LED -> KILL_LED
- U1 pad 15: D_SELECT -> D_SEL
- U2 pad 1: BRAKE_LED -> REV_LED
- U2 pad 108: KILL_LED -> MOTOR_DE
- U2 pad 109: L_PITCH -> R_ROLL
- U2 pad 114: KILL_SWITCH -> MOTOR_EN
- U2 pad 115: unconnected-(U2-PD12-Pad115) -> COL_SENS_2
- U2 pad 116: COL_SENS_8 -> COL_SENS_1
- U2 pad 117: COL_SENS_2 -> COL_SENS_4
- U2 pad 119: COL_SENS_6 -> COL_SENS_3
- U2 pad 123: COL_SENS_4 -> COL_SENS_5
- U2 pad 125: COL_SENS_3 -> COL_SENS_6
- U2 pad 128: COL_SENS_5 -> COL_SENS_8
- U2 pad 130: R_ROLL -> L_ROLL
- U2 pad 2: REV_LED -> BRAKE_LED
- U2 pad 37: R_PITCH -> L_PITCH
- U2 pad 38: L_ROLL -> R_PITCH
- U2 pad 73: MOTOR_DEN -> KILL_LED
- U2 pad 74: MOTOR_EN -> KILL_SWITCH
- U2 pad 75: ASCEND -> DESCEND
- U2 pad 77: DESCEND -> ASCEND
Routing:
- net +5V: track 20.7 -> 1244.9 mm, vias 0 -> 4
- net +3V3: track 17.0 -> 890.6 mm, vias 0 -> 21
- net RESET: track 0.00 -> 305.2 mm, vias 0 -> 3
- net ASCEND_SB: track 0.00 -> 271.9 mm, vias 0 -> 2
- net SWITCH_2_LED: track 0.00 -> 174.1 mm, vias 0 -> 4
- net DESCEND_SB: track 0.00 -> 153.6 mm, vias 0 -> 2
- net SWITCH_2_SB: track 0.00 -> 149.8 mm, vias 0 -> 2
- net R_PITCH: track 0.00 -> 115.4 mm, vias 0 -> 1
- net COL_SENS_1: track 0.00 -> 115.3 mm
- net COL_SENS_4: track 0.00 -> 111.6 mm
- net COL_SENS_2: track 0.00 -> 110.0 mm
- net COL_SENS_3: track 0.00 -> 106.0 mm
- net COL_SENS_6: track 0.00 -> 100.0 mm
- net ASCEND_LED: track 0.00 -> 99.0 mm, vias 0 -> 1
- net MOTOR_MODE_2_SB: track 0.00 -> 98.9 mm
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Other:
- board outline added: 255 x 148.8 mm
